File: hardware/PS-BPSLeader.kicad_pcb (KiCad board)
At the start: 4 copper layers, 100 x 100 mm, 382 parts, among them IC1 TCAN3413DR, IC2 TCAN3413DR, IC3 CYPD3177-24LQXQ, IC4 BQ79600PWRQ1, IC5 LM74502DDFR, IC6 TCAN3413DR, IC7 TPS552872RYQR, J1 USB_C_Receptacle_USB2.0_16P, J10 Low SIde Conn, J11 SWD_Header, J12 SWD, J13 USB_C_Receptacle_USB2.0_16P, J14 Conn_01x02, J15 Contactor Connector, J16 Contactor Connector, J17 Contactor Connector, J2 ELCON CAN DEBUG, J3 ELCON CAN, J4 Conn_02x06_Counter_Clockwise, J5 CAR CAN IN, J6 CAR CAN OUT, J7 BPS CAN DEBUG, J8 BPS CAN, J9 High Side Conn, Q1 SQ2315CES-T1_GE3, Q10 SI7997DP-T1-GE3, Q11 SI7997DP-T1-GE3, Q12 IRLML0030, Q13 PSMN012-100YS, Q14 PSMN012-100YS, Q2 SQ2315CES-T1_GE3, Q3 SQ2315CES-T1_GE3, Q4 IRLML0030, Q5 IRLML0030, Q6 IRLML0030, Q7 IRLML0030, Q8 IRLML0030, Q9 IRLML0030, SW1 SW_SPDT, SW2 BOOT Switch, SW3 RESET Button, T1 HMU1228NL, T2 HMU1228NL, U1 STM32G473VETx, U10 MCP1826S, U11 TPS2117DRLR, U12 LMR51635XDDCR, U13 PESD5V0L2BT, U14 PESD5V0L2BT, U15 TPS2117DRLR, U16 MCP1826S, U17 TPS2121RUXR, U18 CDSOT23-T24CAN, U2 CDSOT23-T24CAN, U3 CDSOT23-T24CAN, U4 ESP32-C6-MINI-1, U5 DRV110APWR, U6 TPS2121RUXR, U7 DRV110APWR, U8 DRV110APWR, U9 EMC2305-1-AP-TR, Y1 Crystal

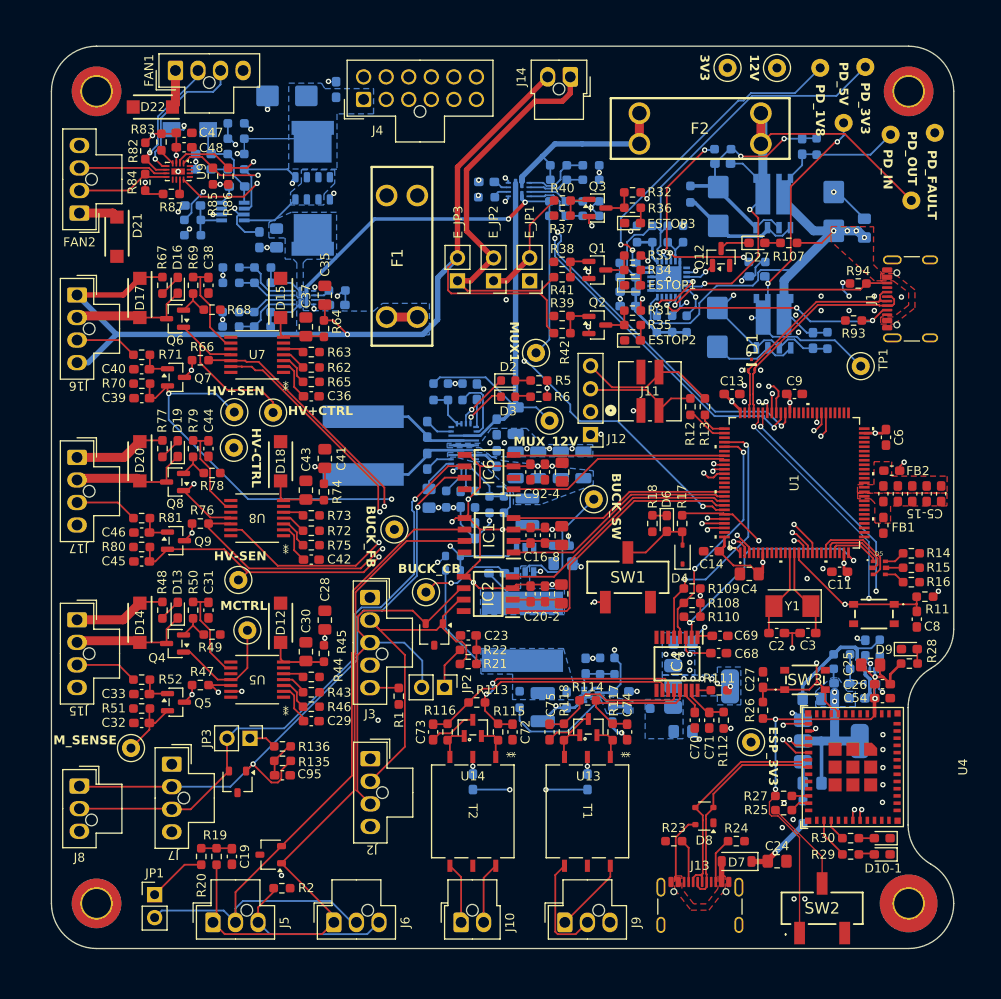
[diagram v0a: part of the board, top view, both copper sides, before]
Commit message: improved some routing, added teardrops
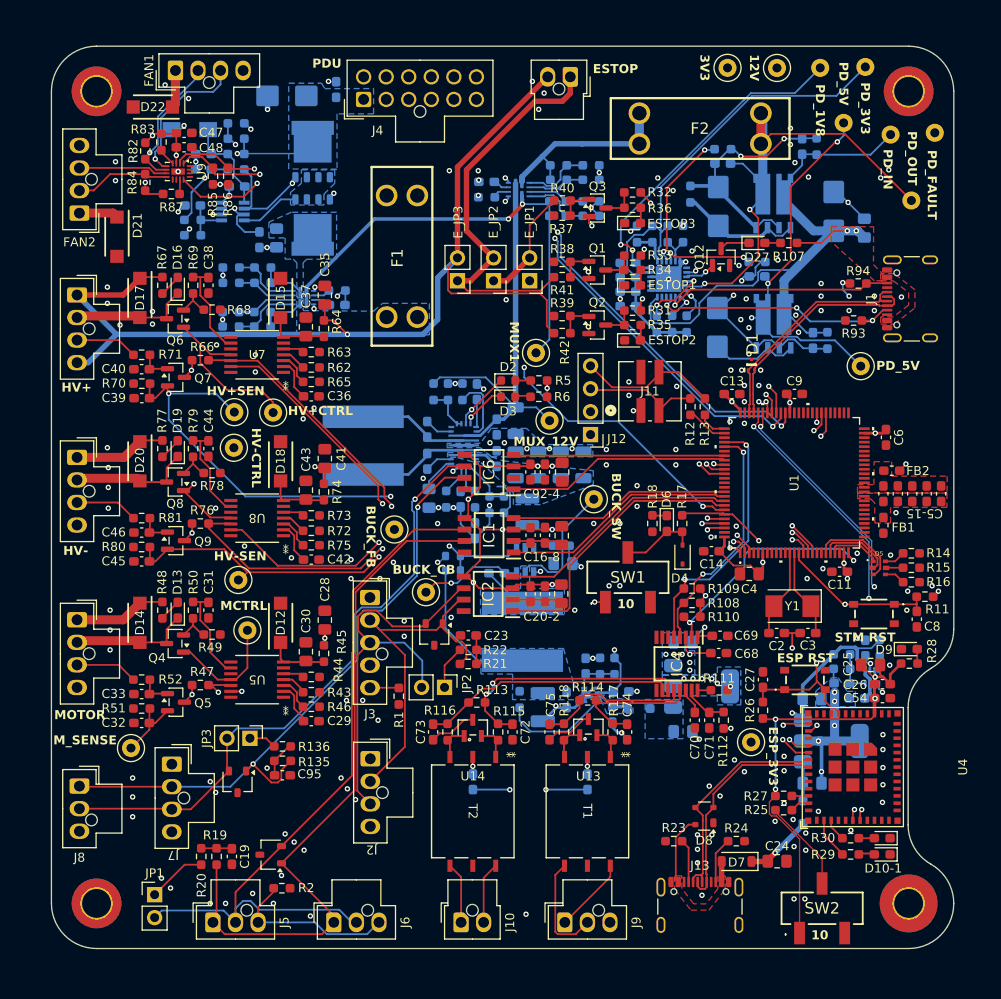
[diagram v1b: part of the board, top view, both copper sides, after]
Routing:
- net /MOTOR_SENSE: track 99.7 -> 106.1 mm
- net GND: track 131.6 -> 136.1 mm, vias 91 -> 211
- net /Power/Power_Mux_PDU_ELCON/Vin2: track 8.65 -> 5.25 mm
- net /MOTOR_CTRL: track 82.8 -> 85.4 mm
- net +3.3V: track 106.0 -> 103.6 mm, vias 38 -> 36
- net /PDU_LV+: track 20.3 -> 22.3 mm
- net /USB_SCL: track 22.7 -> 20.8 mm
- net /HV+_SENSE: track 82.7 -> 84.3 mm
- net /USB_VBUS_IN: track 69.5 -> 71.0 mm, vias 4 -> 2
- net /Power/Power_Mux_PD/Vin1: track 51.7 -> 53.0 mm
- net /ESTOP_2_SENSE: track 28.7 -> 29.7 mm
- net /FAN_SDA: track 82.3 -> 81.3 mm
- net /USB_GPIO: track 22.0 -> 21.1 mm
- net /FAN_SCL: track 83.7 -> 82.8 mm
- net /USB_SDA: track 21.2 -> 22.0 mm
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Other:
- board text added: "10"
- board text added: "ESP RST"
- board text added: "ESTOP"
- board text added: "HV+"
- board text added: "HV-"
- board text added: "MOTOR"
- board text added: "PDU"
- board text added: "STM RST"
